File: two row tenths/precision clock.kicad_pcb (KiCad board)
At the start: 2 copper layers, 157 x 53 mm, 56 parts, among them P1 USB_C_Plug_USB2.0, P2 USB_C_Plug_USB2.0, Q1 MMBT3906, Q2 MMBT3906

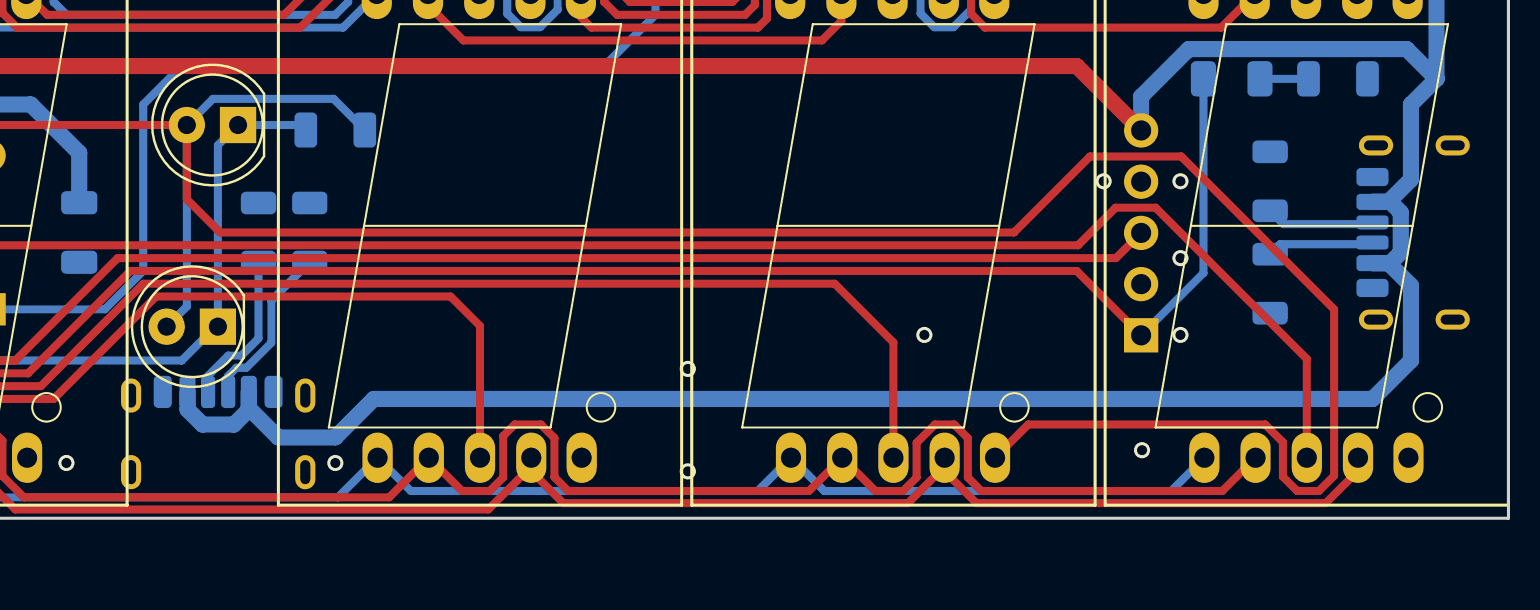
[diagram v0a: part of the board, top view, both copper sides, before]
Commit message: Move over bottom USB connector
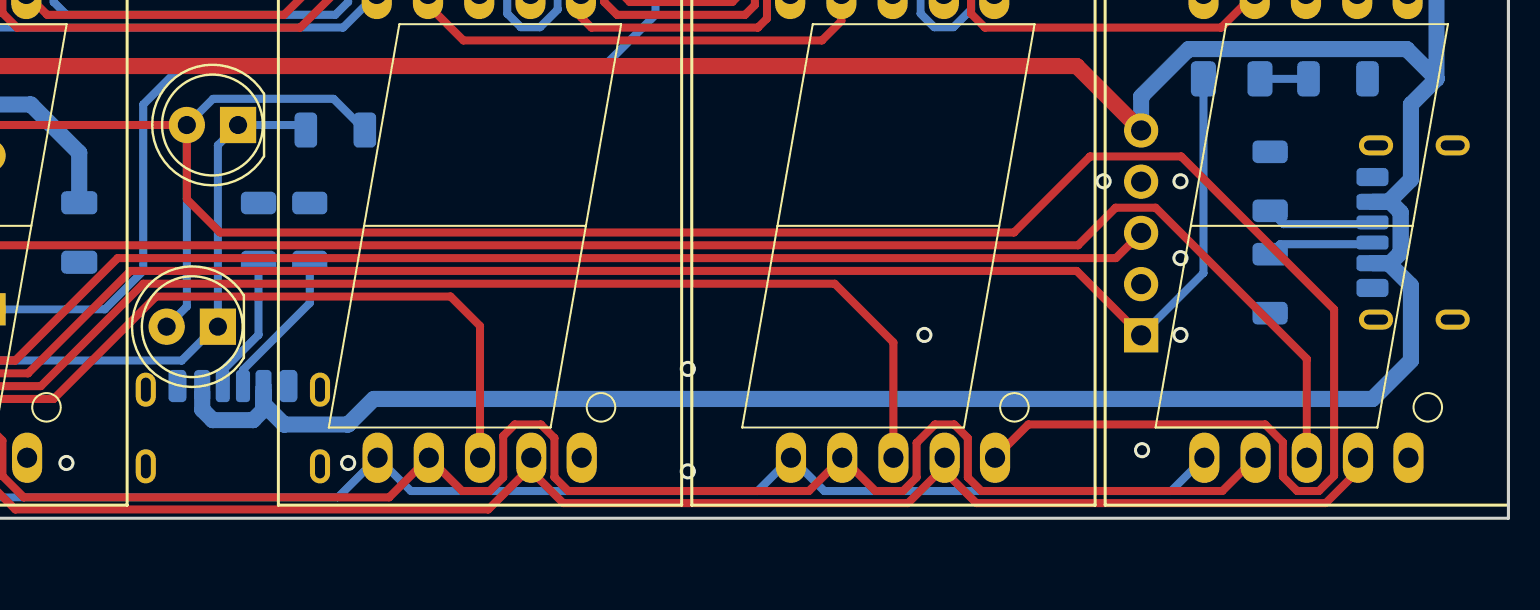
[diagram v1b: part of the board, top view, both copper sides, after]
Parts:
- moved P2 0.79 mm to (118.7, 111.1)
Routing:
- net Net-(P2-CC2): track 7.86 -> 6.89 mm
- net Net-(P2-CC1): track 8.41 -> 7.52 mm
- net +5V: track 402.8 -> 402.3 mm
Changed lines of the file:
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@@
 		(tags "LED")
 		(property "Reference" "D_PPS1"
-			(at 0 -1.905 360)
+			(at 0 -1.905 0)
 			(layer "B.Fab")
 			(effects
@@
 		)
 		(property "Value" "PPS"
-			(at 0 1.905 360)
+			(at 0 1.905 0)
 			(layer "B.SilkS")
 			(effects
@@
 		)
 		(fp_text user "${REFERENCE}"
-			(at 0 0 360)
+			(at 0 0 0)
 			(layer "B.Fab")
 			(effects
@@
 	(footprint "Connector_USB:USB_C_Receptacle_HRO_TYPE-C-31-M-17"
 		(layer "B.Cu")
-		(at 118.015 111.415 180)
+		(at 118.745 111.125 180)
 		(descr "USB Type-C receptacle for USB 2.0, 6 pin, https://omo-oss-file.thefastfile.com/portal-saas/new2023011311465142457/cms/file/134891b2-9b01-4104-89d3-96207243f692.pdf")
 		(tags "usb usb-c 2.0 pd")
@@
 	)
 	(via
-		(at 123.825 111.76)
+		(at 141.305 112.175)
 		(size 0.8)
 		(drill 0.5)
@@
 	)
 	(via
-		(at 141.305 112.175)
+		(at 124.46 111.76)
 		(size 0.8)
 		(drill 0.5)
@@
 	)
 	(segment
+		(start 175.26 108.585)
+		(end 125.73 108.585)
+		(width 0.8)
+		(layer "B.Cu")
+		(net 2)
+	)
+	(segment
 		(start 177.165 93.98)
 		(end 177.165 97.7)
@@
 	)
 	(segment
-		(start 119.535 108.235)
-		(end 119.535 109.035)
+		(start 117.225 109.115864)
+		(end 117.744136 109.635)
+		(width 0.8)
+		(layer "B.Cu")
+		(net 2)
+	)
+	(segment
+		(start 121.285 109.855)
+		(end 120.265 108.835)
+		(width 0.8)
+		(layer "B.Cu")
+		(net 2)
+	)
+	(segment
+		(start 117.225 108.235)
+		(end 117.225 109.115864)
 		(width 0.8)
 		(layer "B.Cu")
@@
 	)
 	(segment
-		(start 116.495 109.115864)
-		(end 117.234136 109.855)
+		(start 175.255 101.85)
+		(end 176.055 101.85)
 		(width 0.8)
 		(layer "B.Cu")
@@
 	)
 	(segment
+		(start 125.73 108.585)
+		(end 124.46 109.855)
+		(width 0.8)
+		(layer "B.Cu")
+		(net 2)
+	)
+	(segment
 		(start 167.64 78.74)
 		(end 167.64 81.71401)
@@
 	)
 	(segment
-		(start 123.825 110.49)
-		(end 125.73 108.585)
+		(start 176.055 101.85)
+		(end 177.165 102.96)
 		(width 0.8)
 		(layer "B.Cu")
@@
 	)
 	(segment
-		(start 175.26 108.585)
+		(start 177.165 102.96)
 		(end 177.165 106.68)
 		(width 0.8)
@@
 	)
 	(segment
+		(start 120.265 109.115864)
+		(end 120.265 108.235)
+		(width 0.8)
+		(layer "B.Cu")
+		(net 2)
+	)
+	(segment
 		(start 163.785 95.27)
 		(end 163.785 93.59099)
@@
 	)
 	(segment
-		(start 176.055 101.85)
-		(end 175.255 101.85)
+		(start 53.34 96.52)
+		(end 55.45 96.52)
 		(width 0.8)
 		(layer "B.Cu")
@@
 	)
 	(segment
-		(start 119.535 109.035)
-		(end 120.99 110.49)
+		(start 171.01599 85.09)
+		(end 176.53 85.09)
 		(width 0.8)
 		(layer "B.Cu")
@@
 	)
 	(segment
-		(start 53.34 96.52)
-		(end 55.45 96.52)
+		(start 107.985 71.12)
+		(end 122.52 71.12)
 		(width 0.8)
 		(layer "B.Cu")
@@
 	)
 	(segment
-		(start 171.01599 85.09)
-		(end 176.53 85.09)
+		(start 120.265 108.835)
+		(end 120.265 107.945)
 		(width 0.8)
 		(layer "B.Cu")
@@
 	)
 	(segment
-		(start 125.73 108.585)
-		(end 175.26 108.585)
+		(start 163.785 93.59099)
+		(end 166.14099 91.235)
 		(width 0.8)
 		(layer "B.Cu")
@@
 	)
 	(segment
-		(start 107.985 71.12)
-		(end 122.52 71.12)
+		(start 111.125 98.855)
+		(end 111.125 96.375786)
 		(width 0.8)
 		(layer "B.Cu")
@@
 	)
 	(segment
-		(start 120.99 110.49)
-		(end 123.825 110.49)
+		(start 53.484214 70.485)
+		(end 53.34 70.485)
 		(width 0.8)
 		(layer "B.Cu")
@@
 	)
 	(segment
-		(start 177.165 102.96)
-		(end 176.055 101.85)
+		(start 120.265 108.235)
+		(end 120.265 108.97796)
 		(width 0.8)
 		(layer "B.Cu")
@@
 	)
 	(segment
-		(start 163.785 93.59099)
-		(end 166.14099 91.235)
+		(start 117.744136 109.635)
+		(end 119.745864 109.635)
 		(width 0.8)
 		(layer "B.Cu")
@@
 	)
 	(segment
-		(start 111.125 98.855)
-		(end 111.125 96.375786)
+		(start 119.745864 109.635)
+		(end 120.265 109.115864)
 		(width 0.8)
 		(layer "B.Cu")
@@
 	)
 	(segment
-		(start 53.484214 70.485)
-		(end 53.34 70.485)
+		(start 178.435 92.71)
+		(end 177.165 93.98)
 		(width 0.8)
 		(layer "B.Cu")
@@
 	)
 	(segment
-		(start 178.435 92.71)
-		(end 177.165 93.98)
+		(start 177.165 106.68)
+		(end 175.26 108.585)
 		(width 0.8)
 		(layer "B.Cu")
@@
 	)
 	(segment
-		(start 117.234136 109.855)
-		(end 118.795864 109.855)
-		(width 0.8)
-		(layer "B.Cu")
-		(net 2)
-	)
-	(segment
-		(start 116.495 108.235)
-		(end 116.495 109.115864)
-		(width 0.8)
-		(layer "B.Cu")
-		(net 2)
-	)
-	(segment
 		(start 176.655 99.329136)
 		(end 176.135864 98.81)
@@
 	)
 	(segment
-		(start 177.165 106.68)
-		(end 177.165 102.96)
-		(width 0.8)
-		(layer "B.Cu")
-		(net 2)
-	)
-	(segment
-		(start 119.535 109.115864)
-		(end 119.535 108.235)
-		(width 0.8)
-		(layer "B.Cu")
-		(net 2)
-	)
-	(segment
-		(start 118.795864 109.855)
-		(end 119.535 109.115864)
+		(start 124.46 109.855)
+		(end 121.285 109.855)
 		(width 0.8)
 		(layer "B.Cu")
@@
 	)
 	(segment
-		(start 104.28 104.14)
-		(end 106.82 106.68)
+		(start 118 96)
+		(end 119 95)
 		(width 0.4)
 		(layer "B.Cu")
@@
 	)
 	(segment
-		(start 116.205 106.68)
-		(end 117.885 105)
+		(start 104.28 104.14)
+		(end 106.82 106.68)
 		(width 0.4)
 		(layer "B.Cu")
@@
 	)
 	(segment
-		(start 118 96)
-		(end 118 105)
+		(start 118 105)
+		(end 118 96)
 		(width 0.4)
 		(layer "B.Cu")
@@
 	)
 	(segment
-		(start 119 95)
-		(end 122.1125 95)
+		(start 116.205 106.68)
+		(end 117.885 105)
 		(width 0.4)
 		(layer "B.Cu")
@@
 	(segment
 		(start 119 95)
-		(end 118 96)
+		(end 122.1125 95)
 		(width 0.4)
 		(layer "B.Cu")
@@
 	)
 	(segment
-		(start 120.65 105.798528)
-		(end 120.65 103.6975)
+		(start 119.245 107.145)
+		(end 122.555 103.835)
 		(width 0.4)
 		(layer "B.Cu")
@@
 	)
 	(segment
-		(start 119.413528 107.035)
-		(end 120.65 105.798528)
+		(start 119.245 107.945)
+		(end 119.245 107.145)
 		(width 0.4)
 		(layer "B.Cu")
@@
 	)
 	(segment
-		(start 118.515 107.435)
-		(end 118.915 107.035)
-		(width 0.4)
-		(layer "B.Cu")
-		(net 98)
-	)
-	(segment
-		(start 120.65 103.6975)
+		(start 122.555 103.835)
 		(end 122.555 101.7925)
 		(width 0.4)
@@
 	)
 	(segment
-		(start 118.915 107.035)
-		(end 119.413528 107.035)
-		(width 0.4)
-		(layer "B.Cu")
-		(net 98)
-	)
-	(segment
-		(start 118.515 108.235)
-		(end 118.515 107.435)
-		(width 0.4)
-		(layer "B.Cu")
-		(net 98)
-	)
-	(segment
 		(start 49.0875 70.2925)
 		(end 50.165 70.2925)
@@
 	)
 	(segment
-		(start 120.015 105.585)
-		(end 120.015 101.7925)
+		(start 118.245 107.945)
+		(end 118.245 107.18)
 		(width 0.4)
 		(layer "B.Cu")
@@
 	)
 	(segment
-		(start 117.515 108.235)
-		(end 117.515 107.435)
-		(width 0.4)
-		(layer "B.Cu")
-		(net 102)
-	)
-	(segment
-		(start 119.165 106.435)
-		(end 120.015 105.585)
-		(width 0.4)
-		(layer "B.Cu")
-		(net 102)
-	)
-	(segment
-		(start 117.515 107.435)
-		(end 118.515 106.435)
+		(start 120.015 105.41)
+		(end 120.015 101.7925)
 		(width 0.4)
 		(layer "B.Cu")
@@
 	)
 	(segment
-		(start 118.515 106.435)
-		(end 119.165 106.435)
+		(start 118.245 107.18)
+		(end 120.015 105.41)
 		(width 0.4)
 		(layer "B.Cu")

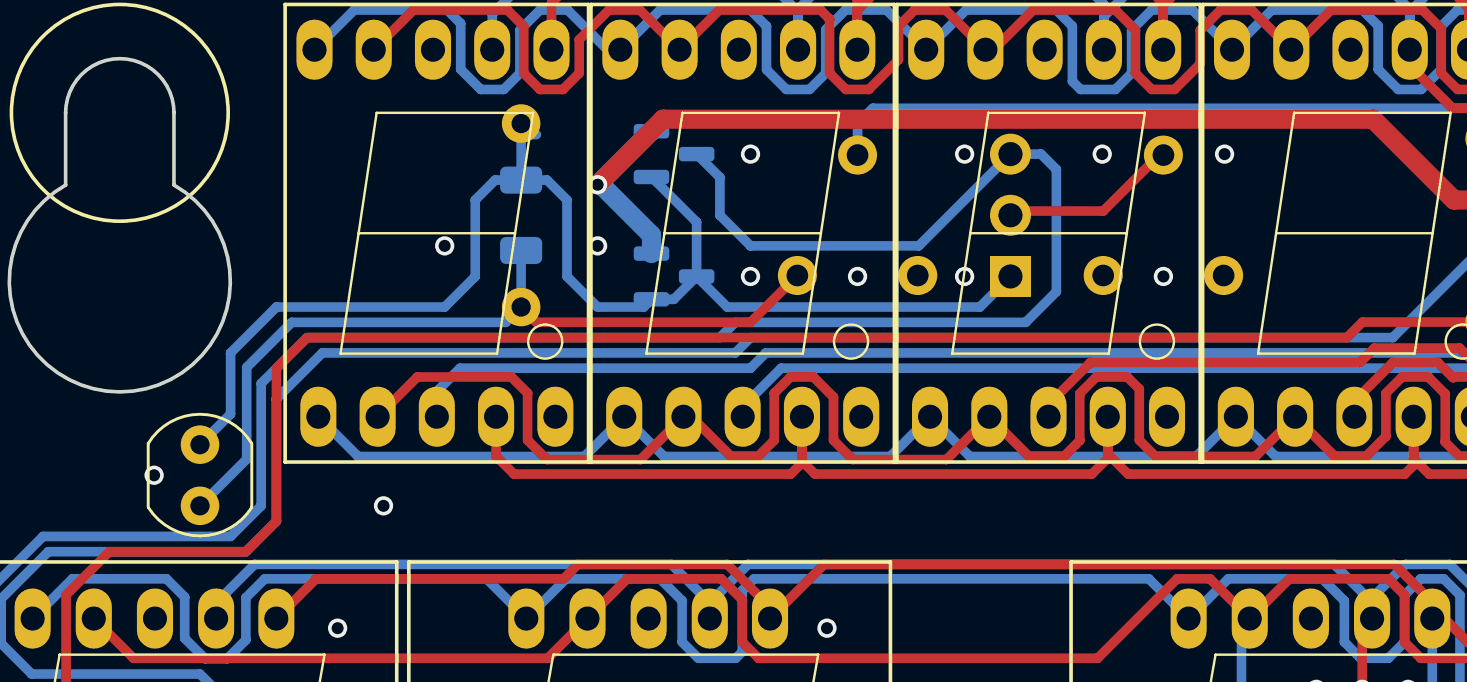
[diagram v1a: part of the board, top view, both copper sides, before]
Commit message: Add resistor so we don't short Q2
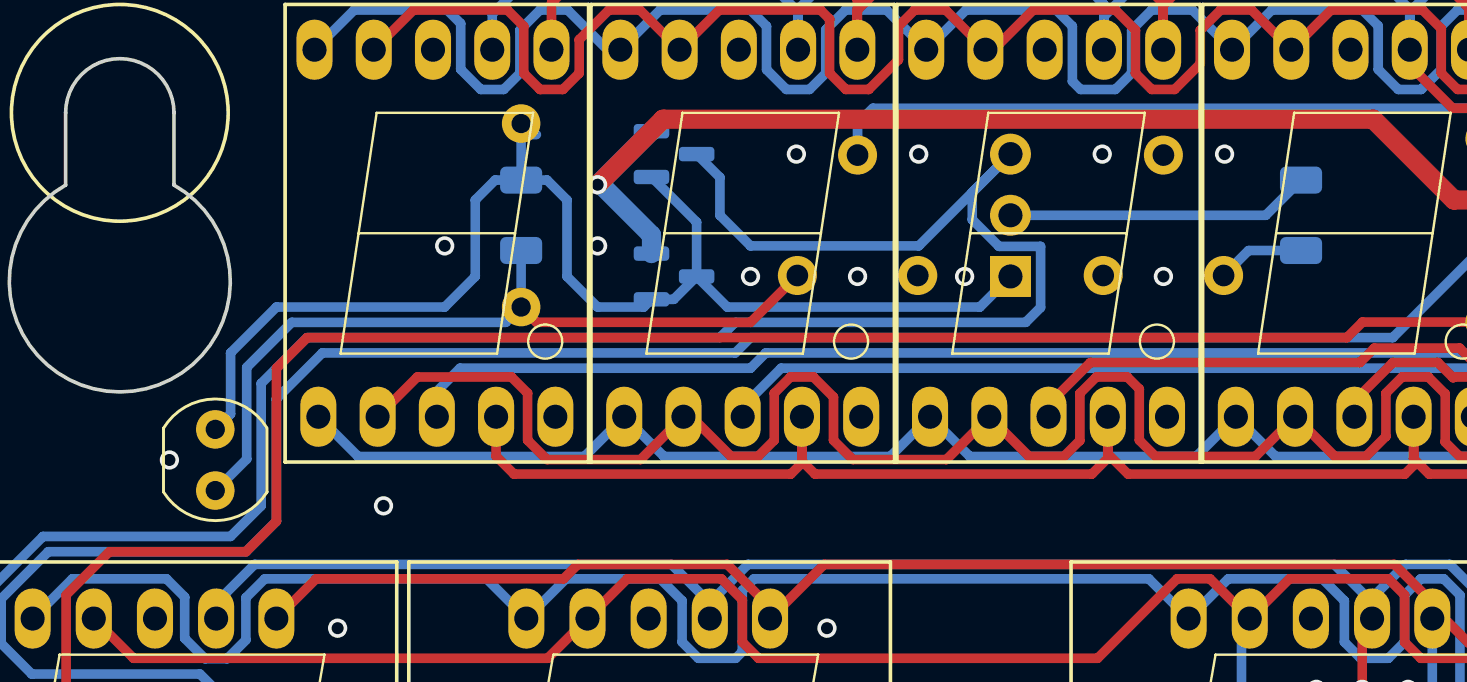
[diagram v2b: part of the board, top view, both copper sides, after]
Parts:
- added R10: 1k, Resistor_SMD:R_1206_3216Metric, B.Cu at (82.5, 71.8)
- C3: value C_Polarized_Small_US -> 100uF
- LDR1: value LDR -> 5537
- R_Min_Bright1, R_Min_Bright2: value 10M -> 100K
- R_Time_brt_adj1: value 100K -> 50K
- moved LDR1 0.90 mm to (37.5, 80.6)
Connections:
- R_Time_brt_adj1 pad 2: Net-(JP1-C) -> GND
- R_Time_brt_adj1 pad 3: unconnected-(R_Time_brt_adj1-Pad3) -> Net-(R10-Pad2)
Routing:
- net Net-(JP1-C): track 7.39 -> 12.7 mm
- net Net-(R10-Pad2): track 0.00 -> 3.64 mm
- net /ISET_TIME: track 151.6 -> 152.7 mm
- net Net-(JP1-A): track 55.1 -> 54.2 mm
- net Net-(LDR1-Pad2): track 33.9 -> 33.0 mm
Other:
- board text added: "Two-row version 1.1 SolidElectronics 2025"
- board text removed: "SolidElectronics 2025"
- board text removed: "Two-row version"

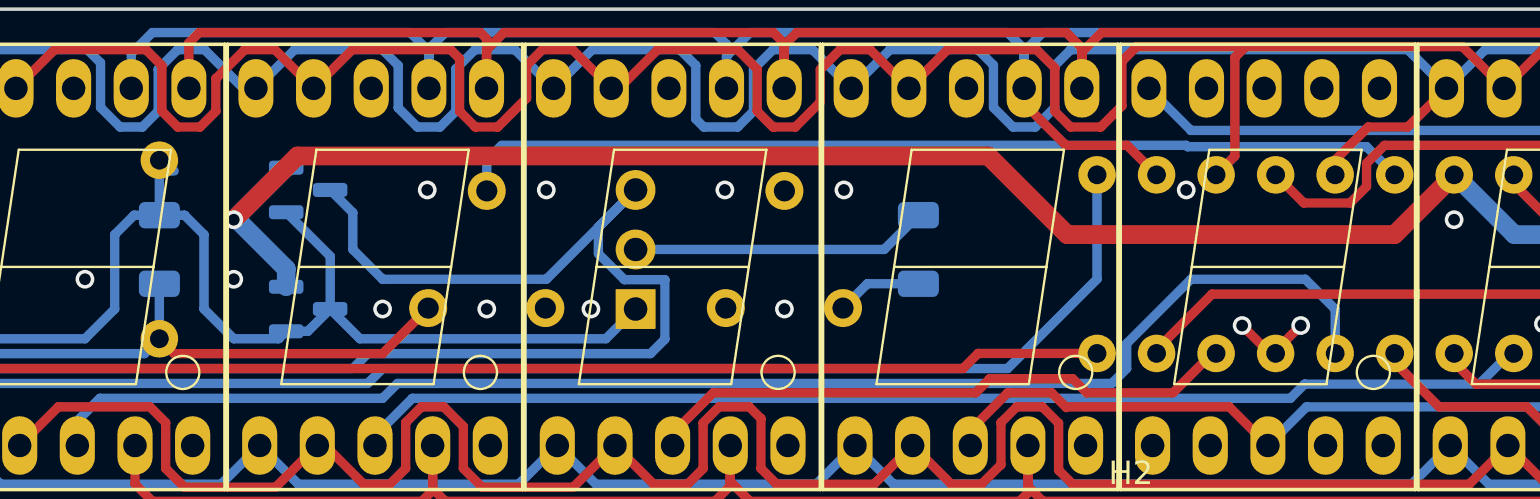
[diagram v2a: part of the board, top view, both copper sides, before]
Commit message: More resistors for brightness tuning
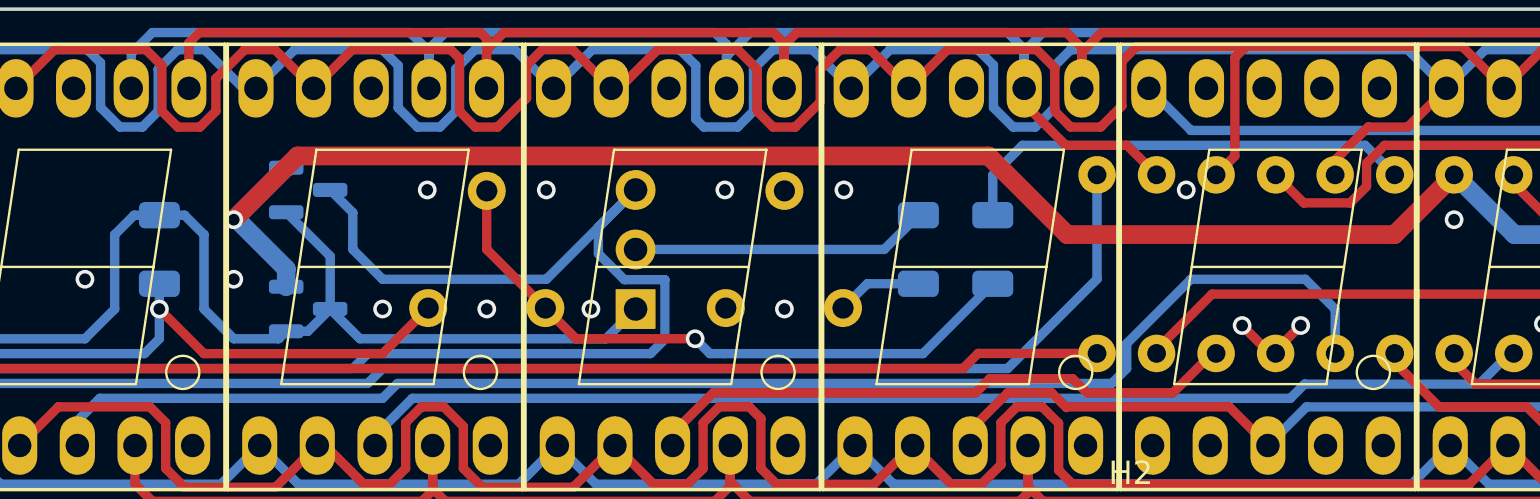
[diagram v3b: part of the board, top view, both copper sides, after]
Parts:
- removed R_Min_Bright1: 100K, Resistor_THT:R_Axial_DIN0207_L6.3mm_D2.5mm_P7.62mm_Horizontal
- added R_MaxBrt1: 33k, Resistor_SMD:R_1206_3216Metric, B.Cu at (85.7, 71.8)
- R10: value 1k -> 4k7
- R_MinBrt1: renamed from R_Min_Bright2; value 100K -> 300K
- renumbered R_Time_brt_adj1 to R_RelBrt1
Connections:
- R_Max_Bright1 pad 2: /ISET_DATE -> Net-(R_MaxBrt1-Pad2)
- R_Max_Bright1 pad 3: unconnected-(R_Max_Bright1-Pad3) -> Net-(R_MaxBrt1-Pad2)
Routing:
- net Net-(R_MaxBrt1-Pad2): track 0.00 -> 27.2 mm, vias 0 -> 1
- net /ISET_DATE: track 40.7 -> 19.9 mm
- net Net-(JP1-A): track 54.2 -> 51.2 mm
- net Net-(LDR1-Pad2): track 33.0 -> 33.5 mm, vias 0 -> 1
